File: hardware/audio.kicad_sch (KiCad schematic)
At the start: 4 parts, among them U9 MAX98357A

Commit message: update bom, correct jlcpcb rotation
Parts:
- U9: JLCPCB Rotation Offset (none) -> 180
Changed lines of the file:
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@@
+			)
+		)
+		(property "JLCPCB Rotation Offset" "180"
+			(at 153.67 96.52 0)
+			(effects
+				(font
+					(size 1.27 1.27)
+				)
+				(hide yes)
 			)
 		)

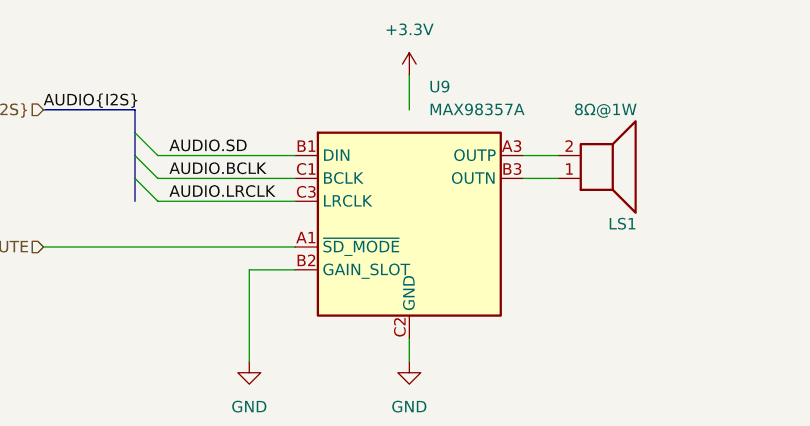
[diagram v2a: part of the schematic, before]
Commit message: Fix audio chip power pin in schematic
Add the motherfucker in project library
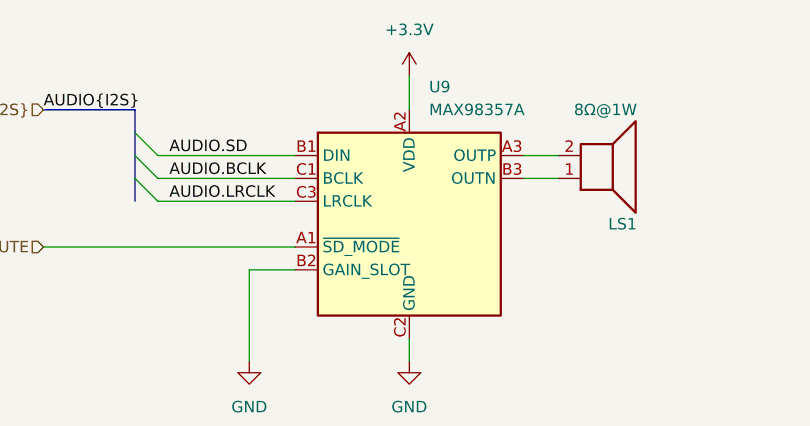
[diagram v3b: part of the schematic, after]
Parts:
- U9: symbol Audio:MAX98357A -> badge:MAX98357A
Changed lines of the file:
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@@
 	)
 	(symbol
-		(lib_id "Audio:MAX98357A")
+		(lib_id "badge:MAX98357A")
 		(at 153.67 96.52 0)
 		(unit 1)

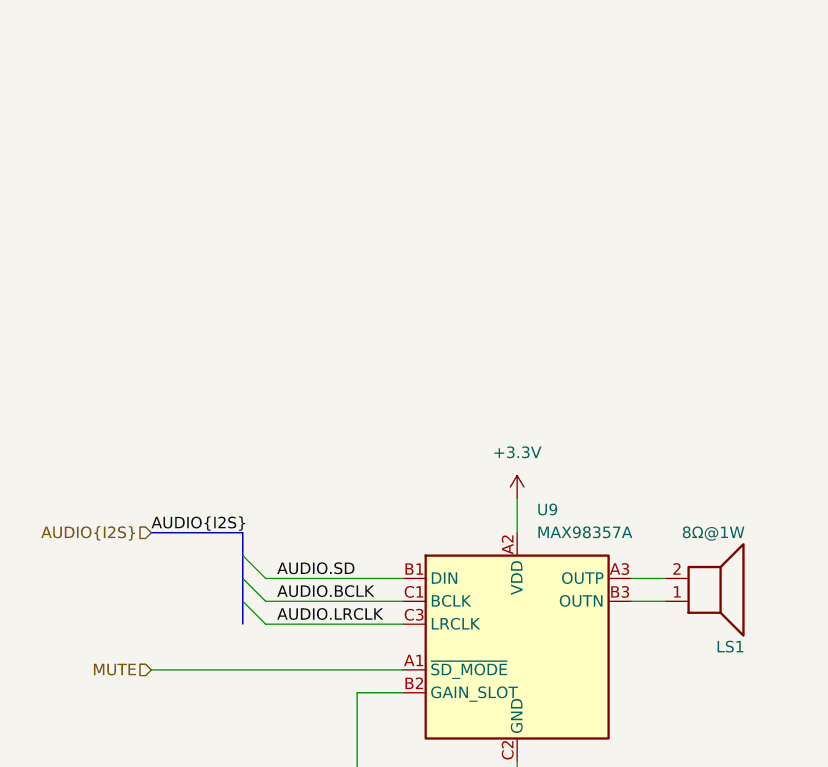
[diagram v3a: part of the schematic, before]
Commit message: dual footprint for audio amp
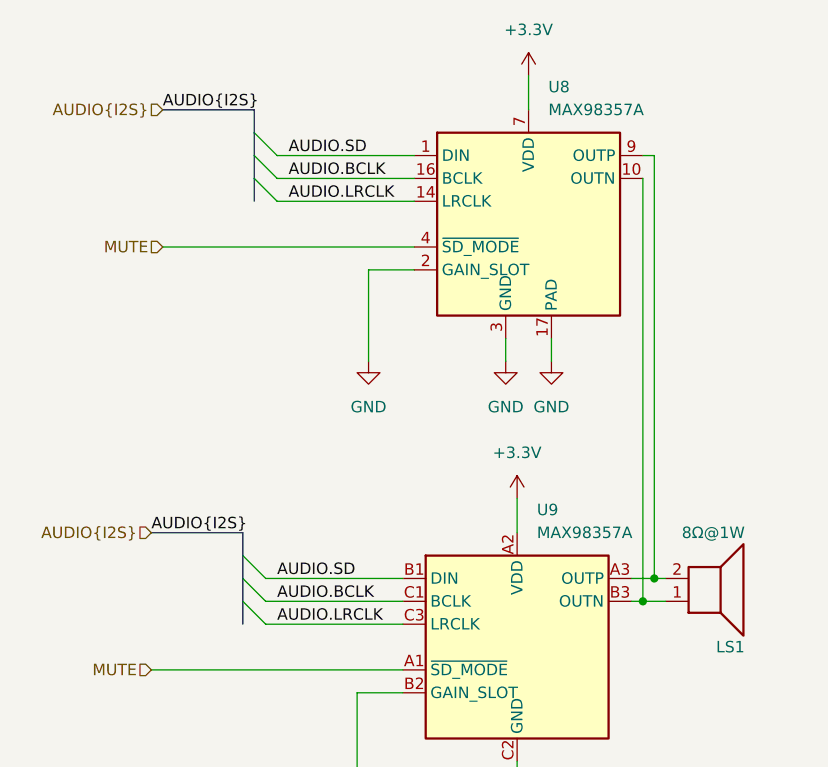
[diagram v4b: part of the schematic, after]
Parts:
- added U8: MAX98357A, Package_DFN_QFN:TQFN-16-1EP_3x3mm_P0.5mm_EP1.23x1.23mm, symbol Audio:MAX98357A
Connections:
- net +3.3V: now also U8.7 (VDD), U8.8 (VDD)
- net AUDIO.BCLK: now also U8.16 (BCLK)
- net AUDIO.LRCLK: now also U8.14 (LRCLK)
- net AUDIO.SD: now also U8.1 (DIN)
- net GND: now also U8.11 (GND), U8.15 (GND), U8.17 (PAD), U8.2 (GAIN_SLOT), U8.3 (GND)
- net MUTE: now also U8.4 (~{SD_MODE})
- net at LS1.2, U9.A3 (OUTP): now also U8.9 (OUTP)
- net at LS1.1, U9.B3 (OUTN): now also U8.10 (OUTN)

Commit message: update lcsc codes to use (new?) basic components
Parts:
- C13: LCSC C1691 -> C19702
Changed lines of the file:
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@@
 			)
 		)
-		(property "LCSC" "C1691"
+		(property "LCSC" "C19702"
 			(at 241.3 147.32 0)
 			(effects
